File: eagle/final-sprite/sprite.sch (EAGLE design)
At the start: 40 parts

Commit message: merged final-sprite changes into master branch
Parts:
- removed 32KHZ: SPRITECRYSTALSPRITECRYSTAL, SpriteCrystal:SPRITECRYSTALSPRITECRYSTAL
- removed ANTENNA1, ANTENNA2: ANTENNA, SpriteAntenna:ANTENNA
- removed C12: 10uF, SparkFun:CAP0805
- removed CC430: CC430F513X---RGZ48, TI_MSP430_v16:CC430F513X---RGZ48
- removed GNDPIN, VCCPIN: SPRITE_PIN, SpritePin:SPRITE_PIN
- removed H-BRIDGE: LV8417CS, lv8417cs:LV8417CS
- removed JP1: (no value), SparkFun:M02PTH
- removed LED1: (no value), SparkFun:LED0603
- removed RECTIFIER: NSR1030QMUTAG, NSR1030QMUTAG:NSR1030QMUTAG
- removed TRISOL1, TRISOL2, TRISOL3, TRISOL4: TRISOLX-WING, TriSolX_QzQube:TRISOLX-WING
- removed TXCO: (no value), SpriteTCXO:TCXO_7Z
- added ANT-N, ANT-P: ANTENNA, SpriteAntenna:ANTENNA
- added D1: (no value), SparkFun:LED0603
- added JP2: (no value), SparkFun:M02PTH
- added P1, P2: SPRITE_PIN, SpritePin:SPRITE_PIN
- added S1, S2, S3, S4: TRISOLX-WING, TriSolX_QzQube:TRISOLX-WING
- added U$1: UMAC, UMAC:UMAC
- added U$4: ADP5092, STAC:ADP5092
- added U1: CC430F5137, TI_MSP430_v16:CC430F513X---RGZ48
- added X1: TCXO_7Z, SpriteTCXO:TCXO_7Z
- C1: value 0.1uF -> 10 nF; device SparkFun:CAP0805 -> SparkFun:CAP0603-CAP
- C10: value 470nF -> 0.1uF
- C11: value 10nF -> 10uF
- C2: value 10nF -> 470nF; device SparkFun:CAP0805 -> SparkFun:CAP0603-CAP
- C3: value 0.1uF -> 470nF; device SparkFun:CAP0805 -> SparkFun:CAP0603-CAP
- C4: value 0.1uF -> 2.2nF; device SparkFun:CAP0805 -> SparkFun:CAP0603-CAP
- C5: value 10uF -> 10nF; device SparkFun:CAP0805 -> SparkFun:CAP0603-CAP
- C6: value 470nF -> 100nF; device SparkFun:CAP0805 -> SparkFun:CAP0603-CAP
- C7: value 10uF -> 0.1uF
- L1: value 12nH -> 12 nH; device SparkFun:INDUCTOR0402 -> SparkFun:INDUCTOR0603
- R1: value 10K -> 56K; device SparkFun:RESISTOR0805-RES -> SparkFun:RESISTOR0603-RES
- R2: value 10K -> 47K; device SparkFun:RESISTOR0805-RES -> SparkFun:RESISTOR0603-RES
- R5: value 10K -> 270R; device SparkFun:RESISTOR0805-RES -> SparkFun:RESISTOR0603-RES
- R6, R7: value 56K -> 10K
- R8: value 1K -> 10K
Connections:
- removed net #RST/SBWTDIO: CC430.40, JP3.1, R7.2
- removed net ANT1: ANTENNA1.IN, CC430.29
- removed net ANT2: ANTENNA2.IN, CC430.30
- removed net COIL1: H-BRIDGE.OUT1, R8.1, RECTIFIER.PIN1
- removed net GUARD: C10.1, C8.1, C9.1, CC430.27, CC430.28, CC430.31, CC430.32, CC430.34, L1.2
- removed net LOADLINE: H-BRIDGE.OUT2, R8.2, RECTIFIER.PIN3
- removed net N$8: 32KHZ.PIN1, CC430.43
- removed net P1.0: CC430.13
- removed net P1.1: CC430.12
- removed net P1.2: CC430.11
- removed net P1.7: CC430.4
- removed net P2.1/A1: CC430.2
- removed net P2.2/A2: CC430.1
- removed net P2.2/A4: CC430.47
- removed net P2.3/A3: CC430.48
- removed net P2.6: CC430.24
- removed net P2.7: CC430.23, H-BRIDGE.IN2
- removed net P3.0: CC430.21, H-BRIDGE.IN1
- removed net P3.1: CC430.20, H-BRIDGE.ENA
- removed net P3.2: CC430.19
- removed net P3.3: CC430.18
- removed net P3.4: CC430.17
- removed net P3.5: CC430.16
- removed net P3.6: CC430.15
- removed net P3.7: CC430.14, LED1.A
- removed net R_BIAS: CC430.33, R6.2
- removed net TCK_PJ.3: CC430.38
- removed net TDI_PJ.1: CC430.36
- removed net TDO_PJ.0: CC430.35
- removed net TEST/SBWTCK: CC430.39, JP3.2
- removed net TMS_PJ.2: CC430.37
- removed net VCORE: C6.2, CC430.7
- new net N$11: D1.A, R5.1
- new net N$12: C1.2, X1.OUT
- new net N$6: C8.1, LSM9DS1.CAP
- new net PGOOD: U$4.PGOOD
- new net REGGOOD: U$4.REGGOOD
- new net RF_N: ANT-N.IN, U1.30
- new net RF_P: ANT-P.IN, U1.29
- new net RST: C4.2, JP2.1, R2.1, U1.40
- new net TST: JP2.2, U1.39
- new net VBAT: U$1.V+, U$4.BAT
- new net VCCA: C5.1, C6.1, L1.2, U1.27, U1.28, U1.31, U1.32
- new net VCCINT: S1.C, S2.C, S3.C, S4.C
- new net VCCIO: U$4.REGFB, U$4.REG_OUT
- net GND: now also C11.2, C4.1, C6.2, C7.2, D1.C, P2.PIN, R1.2, R7.1, R8.1, S1.A, S2.A, S3.A, S4.A, U$1.V-, U$4.AGND, U$4.GND, U$4.PGND, U1.42, U1.49, X1.GND; no longer C1.2, C12.1, C4.2, C6.1, C7.1, CC430.42, CC430.49, GNDPIN.P$1, H-BRIDGE.PGND, H-BRIDGE.SGND, LED1.C, R4.1, R5.1, R6.1, RECTIFIER.GND, TRISOL1.A, TRISOL2.A, TRISOL3.A, TRISOL4.A, TXCO.GND
- net N$1: now also U1.25; no longer LSM9DS1.C1
- net N$2: now also R5.2, U1.14; no longer C2.1, LSM9DS1.CAP
- net N$3: now also U1.33; no longer LSM9DS1.CS_A/G, LSM9DS1.CS_M, LSM9DS1.SDO_A/G, LSM9DS1.SDO_M
- net N$4: now also C3.1, U1.7; no longer C11.1, CC430.25
- net N$5: now also C7.1, LSM9DS1.C1; no longer C11.2, TXCO.OUT
- net N$7: now also LSM9DS1.CS_A/G, LSM9DS1.CS_M, LSM9DS1.SDO_A/G, LSM9DS1.SDO_M, R3.1; no longer 32KHZ.PIN2, CC430.44
- net P2.0/A0: now also R7.2; no longer CC430.3, R4.2
- net P2.5/A5: now also R8.2; no longer CC430.46, R5.2
- net SCL: now also R6.1, U1.9; no longer CC430.9, R3.1
- net SDA: now also R4.1, U1.10; no longer CC430.10, R2.1
- net UART_RX: now also JP3.2, U1.6; no longer CC430.6, JP1.2
- net UART_TX: now also JP3.1, U1.5; no longer CC430.5, JP1.1
- net VCC: now also C10.1, C11.1, C2.1, C9.1, P1.PIN, R4.2, R6.2, U$4.SYS, U1.22, U1.34, U1.41, U1.45, U1.8, X1.VCC; no longer C12.2, C3.1, C4.1, C5.1, C7.2, CC430.22, CC430.41, CC430.45, CC430.8, H-BRIDGE.VCC, H-BRIDGE.VM, R1.2, R7.1, RECTIFIER.VCC, TRISOL1.C, TRISOL2.C, TRISOL3.C, TRISOL4.C, TXCO.VCC, VCCPIN.P$1
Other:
- note added: "CORE:"
- note added: "Power"
- note added: "Torque Coils"
- note removed: "Antennae"
- note removed: "CDH/T&C:"
- note removed: "Inductive Powering/Torque Coils"
- note removed: "Power/Attitude Control:"
- note removed: "The CC430 serves as both flight computer and radio. It is connected via I2C to the LSM9DS1 and via analog input to the two sun sensors (phototransistors). The MCU is also connected to an external 32.678 kHz oscillator, and a 26 MHz clock. The layout is schematically identical to a PanStamp NRG 2, and is programmable via SBW or serial. The CC430 connects with the dipole antennae."
- note removed: "The LMS9DS1 is connected via I2C to the CC430. The chip includes a magnetometer (3-axis), an accelerometer (3-axis), and a gyroscope (3-axis). SparkFun has written supporting Arduino libraries. The sun sensors are two ALS-PT19-315C ambient light sensors"
- note removed: "The board features four TriSolX solar panels, along with a set of inductive coils and a full bridge rectifier for inductive powering. The inductive coils double as torque coils, controlled via four of the CC430 pins connected to an H-bridge."
- note removed: "The output pins of the H-Bridge are connected with the coils as the load. The coils are connected in parallel to the full bridge rectifier circuit."
- note removed: "TriSolX Solar Panels"

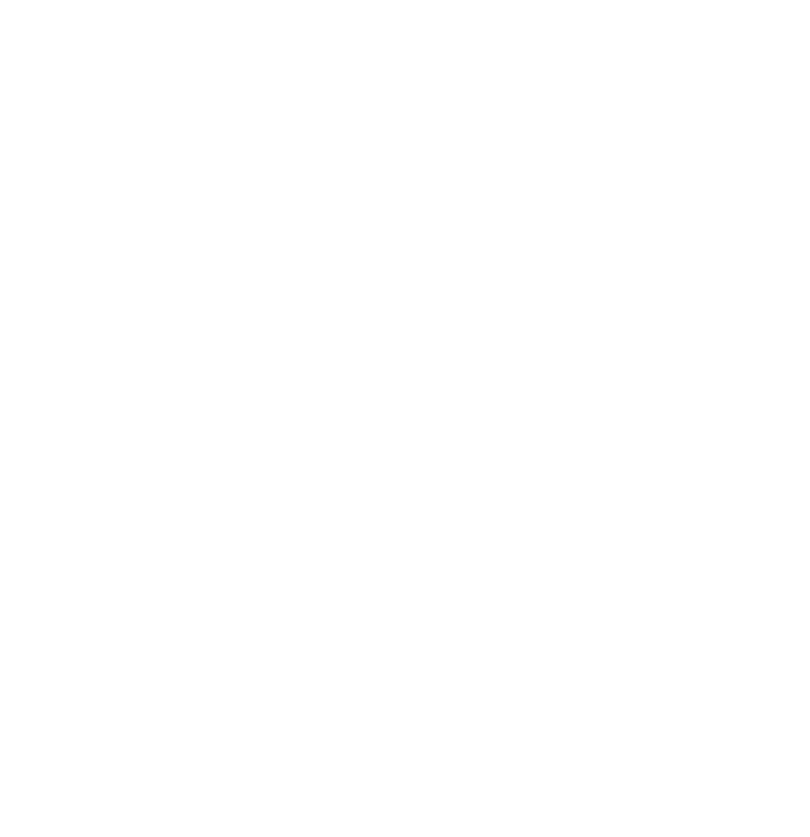
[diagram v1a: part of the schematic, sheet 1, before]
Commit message: Add DRV8833CRTER
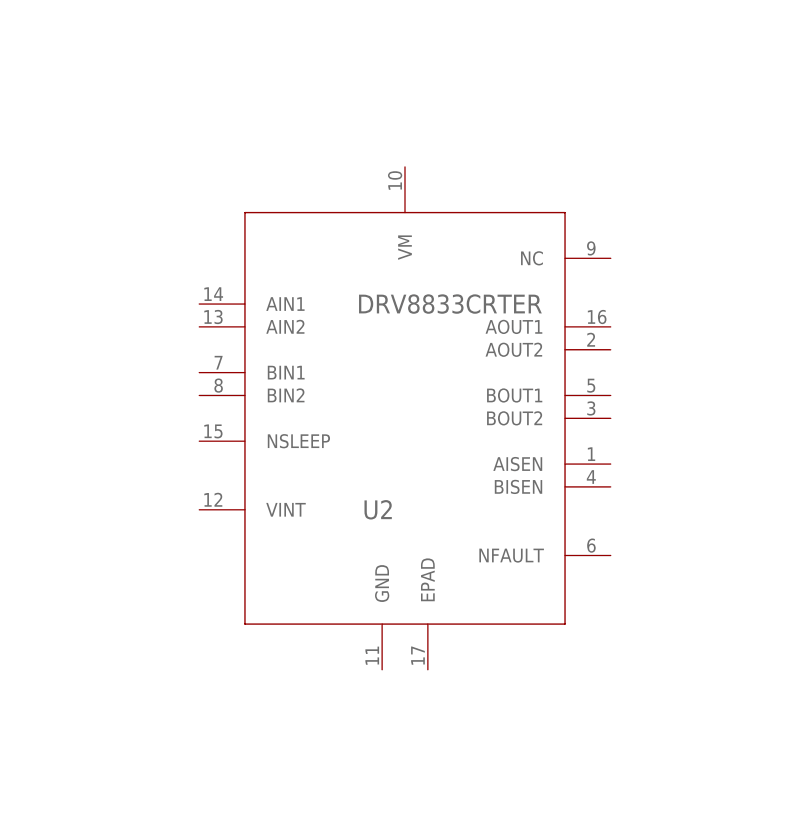
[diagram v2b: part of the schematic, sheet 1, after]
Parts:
- added U2: DRV8833CRTER, STAC:DRV8833CRTER
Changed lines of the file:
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@@
 <?xml version="1.0" encoding="utf-8"?>
 <!DOCTYPE eagle SYSTEM "eagle.dtd">
-<eagle version="9.0.1">
+<eagle version="9.0.0">
 <drawing>
 <settings>
@@
 <part name="P+1" library="SparkFun" deviceset="VCC" device=""/>
 <part name="SUPPLY1" library="SparkFun-PowerSymbols" library_urn="urn:adsk.eagle:library:530" deviceset="VCCIO" device=""/>
+<part name="U2" library="STAC" deviceset="DRV8833CRTER" device=""/>
 </parts>
 <sheets>
@@
 <instance part="P+1" gate="1" x="226.06" y="-78.74"/>
 <instance part="SUPPLY1" gate="G$1" x="220.98" y="-78.74"/>
+<instance part="U2" gate="A" x="203.2" y="-218.44"/>
 </instances>
 <busses>

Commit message: Place COIL?_IN? pins
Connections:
- new net COIL1_IN1: U1.20
- new net COIL1_IN2: U1.19
- new net COIL2_IN1: U1.18
- new net COIL2_IN2: U1.17
- new net COIL3_IN1: U1.2
- new net COIL3_IN2: U1.1
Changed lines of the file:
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@@
+</segment>
+</net>
+<net name="COIL1_IN1" class="0">
+<segment>
+<pinref part="U1" gate="G$1" pin="20"/>
+<wire x1="-20.32" y1="-236.22" x2="-33.02" y2="-236.22" width="0.1524" layer="91"/>
+<label x="-33.02" y="-236.22" size="1.778" layer="95"/>
+</segment>
+</net>
+<net name="COIL1_IN2" class="0">
+<segment>
+<pinref part="U1" gate="G$1" pin="19"/>
+<wire x1="-20.32" y1="-233.68" x2="-33.02" y2="-233.68" width="0.1524" layer="91"/>
+<label x="-33.02" y="-233.68" size="1.778" layer="95"/>
+</segment>
+</net>
+<net name="COIL2_IN1" class="0">
+<segment>
+<pinref part="U1" gate="G$1" pin="18"/>
+<wire x1="-20.32" y1="-231.14" x2="-33.02" y2="-231.14" width="0.1524" layer="91"/>
+<label x="-33.02" y="-231.14" size="1.778" layer="95"/>
+</segment>
+</net>
+<net name="COIL2_IN2" class="0">
+<segment>
+<pinref part="U1" gate="G$1" pin="17"/>
+<wire x1="-20.32" y1="-228.6" x2="-33.02" y2="-228.6" width="0.1524" layer="91"/>
+<label x="-33.02" y="-228.6" size="1.778" layer="95"/>
+</segment>
+</net>
+<net name="COIL3_IN1" class="0">
+<segment>
+<pinref part="U1" gate="G$1" pin="2"/>
+<wire x1="-20.32" y1="-190.5" x2="-33.02" y2="-190.5" width="0.1524" layer="91"/>
+<label x="-33.02" y="-190.5" size="1.778" layer="95"/>
+</segment>
+</net>
+<net name="COIL3_IN2" class="0">
+<segment>
+<pinref part="U1" gate="G$1" pin="1"/>
+<wire x1="-20.32" y1="-187.96" x2="-33.02" y2="-187.96" width="0.1524" layer="91"/>
+<label x="-33.02" y="-187.96" size="1.778" layer="95"/>
 </segment>
 </net>

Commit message: More progress on COIL12
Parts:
- added C12: 10uF, SparkFun:CAP0603-CAP
- added C13: 2.2uF, SparkFun:CAP0603-CAP
- added R10, R9: 270R, SparkFun:RESISTOR0603-RES
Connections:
- new net COIL12_EN: U1.16, U2.NSLEEP
- new net COIL12_FAULT: U1.13, U2.NFAULT
- new net COIL3_EN: U1.48
- new net COIL3_FAULT: U1.12
- new net N$10: R10.2, U2.AISEN
- new net N$8: C13.1, U2.VINT
- new net N$9: R9.2, U2.BISEN
- net COIL1_IN1: now also U2.AIN1
- net COIL1_IN2: now also U2.AIN2
- net COIL2_IN1: now also U2.BIN1
- net COIL2_IN2: now also U2.BIN2
- net GND: now also C12.2, C13.2, R10.1, R9.1, U2.EPAD, U2.GND
- net VCCIO: now also C12.1, U2.VM
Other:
- note added: "Rated up to VCCIO"
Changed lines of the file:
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@@
 <part name="SUPPLY1" library="SparkFun-PowerSymbols" library_urn="urn:adsk.eagle:library:530" deviceset="VCCIO" device=""/>
 <part name="U2" library="STAC" deviceset="DRV8833CRTER" device=""/>
+<part name="GND17" library="SparkFun" deviceset="GND" device=""/>
+<part name="SUPPLY2" library="SparkFun-PowerSymbols" library_urn="urn:adsk.eagle:library:530" deviceset="VCCIO" device=""/>
+<part name="C12" library="SparkFun" deviceset="CAP" device="0603-CAP" value="10uF"/>
+<part name="GND18" library="SparkFun" deviceset="GND" device=""/>
+<part name="C13" library="SparkFun" deviceset="CAP" device="0603-CAP" value="2.2uF"/>
+<part name="GND19" library="SparkFun" deviceset="GND" device=""/>
+<part name="R9" library="SparkFun" deviceset="RESISTOR" device="0603-RES" value="270R"/>
+<part name="R10" library="SparkFun" deviceset="RESISTOR" device="0603-RES" value="270R"/>
+<part name="GND24" library="SparkFun" deviceset="GND" device=""/>
+<part name="GND25" library="SparkFun" deviceset="GND" device=""/>
 </parts>
 <sheets>
@@
 <text x="152.4" y="-73.66" size="5.08" layer="97">Power</text>
 <wire x1="149.86" y1="-167.64" x2="304.8" y2="-167.64" width="0.6096" layer="97" style="longdash"/>
+<text x="187.96" y="-248.92" size="1.778" layer="91">Rated up to VCCIO</text>
 </plain>
 <instances>
@@
 <instance part="SUPPLY1" gate="G$1" x="220.98" y="-78.74"/>
 <instance part="U2" gate="A" x="203.2" y="-218.44"/>
+<instance part="GND17" gate="1" x="228.6" y="-269.24" rot="MR0"/>
+<instance part="SUPPLY2" gate="G$1" x="213.36" y="-195.58"/>
+<instance part="C12" gate="G$1" x="213.36" y="-200.66"/>
+<instance part="GND18" gate="1" x="213.36" y="-205.74" rot="MR0"/>
+<instance part="C13" gate="G$1" x="198.12" y="-254"/>
+<instance part="GND19" gate="1" x="198.12" y="-259.08" rot="MR0"/>
+<instance part="R9" gate="G$1" x="256.54" y="-259.08" rot="R90"/>
+<instance part="R10" gate="G$1" x="266.7" y="-256.54" rot="R90"/>
+<instance part="GND24" gate="1" x="256.54" y="-269.24" rot="MR0"/>
+<instance part="GND25" gate="1" x="266.7" y="-269.24" rot="MR0"/>
 </instances>
 <busses>
@@
 <pinref part="GND3" gate="1" pin="GND"/>
 </segment>
+<segment>
+<pinref part="U2" gate="A" pin="GND"/>
+<wire x1="226.06" y1="-261.62" x2="226.06" y2="-264.16" width="0.1524" layer="91"/>
+<wire x1="226.06" y1="-264.16" x2="228.6" y2="-264.16" width="0.1524" layer="91"/>
+<pinref part="U2" gate="A" pin="EPAD"/>
+<wire x1="228.6" y1="-264.16" x2="231.14" y2="-264.16" width="0.1524" layer="91"/>
+<wire x1="231.14" y1="-264.16" x2="231.14" y2="-261.62" width="0.1524" layer="91"/>
+<wire x1="228.6" y1="-264.16" x2="228.6" y2="-266.7" width="0.1524" layer="91"/>
+<pinref part="GND17" gate="1" pin="GND"/>
+</segment>
+<segment>
+<pinref part="C12" gate="G$1" pin="2"/>
+<pinref part="GND18" gate="1" pin="GND"/>
+</segment>
+<segment>
+<pinref part="C13" gate="G$1" pin="2"/>
+<pinref part="GND19" gate="1" pin="GND"/>
+</segment>
+<segment>
+<pinref part="R9" gate="G$1" pin="1"/>
+<pinref part="GND24" gate="1" pin="GND"/>
+<wire x1="256.54" y1="-264.16" x2="256.54" y2="-266.7" width="0.1524" layer="91"/>
+</segment>
+<segment>
+<pinref part="R10" gate="G$1" pin="1"/>
+<pinref part="GND25" gate="1" pin="GND"/>
+<wire x1="266.7" y1="-261.62" x2="266.7" y2="-266.7" width="0.1524" layer="91"/>
+</segment>
 </net>
 <net name="UART_RX" class="0">
@@
 <pinref part="SUPPLY1" gate="G$1" pin="VCCIO"/>
 </segment>
+<segment>
+<pinref part="C12" gate="G$1" pin="1"/>
+<pinref part="SUPPLY2" gate="G$1" pin="VCCIO"/>
+<wire x1="213.36" y1="-195.58" x2="228.6" y2="-195.58" width="0.1524" layer="91"/>
+<pinref part="U2" gate="A" pin="VM"/>
+<wire x1="228.6" y1="-195.58" x2="228.6" y2="-205.74" width="0.1524" layer="91"/>
+</segment>
 </net>
 <net name="COIL1_IN1" class="0">
@@
 <label x="-33.02" y="-236.22" size="1.778" layer="95"/>
 </segment>
+<segment>
+<pinref part="U2" gate="A" pin="AIN1"/>
+<wire x1="205.74" y1="-220.98" x2="187.96" y2="-220.98" width="0.1524" layer="91"/>
+<label x="187.96" y="-220.98" size="1.778" layer="95"/>
+</segment>
 </net>
 <net name="COIL1_IN2" class="0">
@@
 <label x="-33.02" y="-233.68" size="1.778" layer="95"/>
 </segment>
+<segment>
+<pinref part="U2" gate="A" pin="AIN2"/>
+<wire x1="205.74" y1="-223.52" x2="187.96" y2="-223.52" width="0.1524" layer="91"/>
+<label x="187.96" y="-223.52" size="1.778" layer="95"/>
+</segment>
 </net>
 <net name="COIL2_IN1" class="0">
@@
 <label x="-33.02" y="-231.14" size="1.778" layer="95"/>
 </segment>
+<segment>
+<pinref part="U2" gate="A" pin="BIN1"/>
+<wire x1="205.74" y1="-228.6" x2="187.96" y2="-228.6" width="0.1524" layer="91"/>
+<label x="187.96" y="-228.6" size="1.778" layer="95"/>
+</segment>
 </net>
 <net name="COIL2_IN2" class="0">
@@
 <label x="-33.02" y="-228.6" size="1.778" layer="95"/>
 </segment>
+<segment>
+<pinref part="U2" gate="A" pin="BIN2"/>
+<wire x1="205.74" y1="-231.14" x2="187.96" y2="-231.14" width="0.1524" layer="91"/>
+<label x="187.96" y="-231.14" size="1.778" layer="95"/>
+</segment>
 </net>
 <net name="COIL3_IN1" class="0">
@@
 </segment>
 </net>
+<net name="N$8" class="0">
+<segment>
+<pinref part="C13" gate="G$1" pin="1"/>
+<wire x1="198.12" y1="-248.92" x2="198.12" y2="-243.84" width="0.1524" layer="91"/>
+<pinref part="U2" gate="A" pin="VINT"/>
+<wire x1="198.12" y1="-243.84" x2="205.74" y2="-243.84" width="0.1524" layer="91"/>
+</segment>
+</net>
+<net name="COIL12_EN" class="0">
+<segment>
+<pinref part="U1" gate="G$1" pin="16"/>
+<wire x1="-20.32" y1="-226.06" x2="-33.02" y2="-226.06" width="0.1524" layer="91"/>
+<label x="-33.02" y="-226.06" size="1.778" layer="95"/>
+</segment>
+<segment>
+<pinref part="U2" gate="A" pin="NSLEEP"/>
+<wire x1="205.74" y1="-236.22" x2="187.96" y2="-236.22" width="0.1524" layer="91"/>
+<label x="187.96" y="-236.22" size="1.778" layer="95"/>
+</segment>
+</net>
+<net name="COIL3_EN" class="0">
+<segment>
+<pinref part="U1" gate="G$1" pin="48"/>
+<wire x1="25.4" y1="-187.96" x2="40.64" y2="-187.96" width="0.1524" layer="91"/>
+<label x="30.48" y="-187.96" size="1.778" layer="95"/>
+</segment>
+</net>
+<net name="COIL12_FAULT" class="0">
+<segment>
+<pinref part="U1" gate="G$1" pin="13"/>
+<wire x1="-20.32" y1="-218.44" x2="-38.1" y2="-218.44" width="0.1524" layer="91"/>
+<label x="-38.1" y="-218.44" size="1.778" layer="95"/>
+</segment>
+<segment>
+<pinref part="U2" gate="A" pin="NFAULT"/>
+<wire x1="251.46" y1="-248.92" x2="279.4" y2="-248.92" width="0.1524" layer="91"/>
+<label x="287.02" y="-246.38" size="1.778" layer="95" rot="R180"/>
+<wire x1="279.4" y1="-248.92" x2="287.02" y2="-248.92" width="0.1524" layer="91"/>
+</segment>
+</net>
+<net name="COIL3_FAULT" class="0">
+<segment>
+<pinref part="U1" gate="G$1" pin="12"/>
+<wire x1="-20.32" y1="-215.9" x2="-38.1" y2="-215.9" width="0.1524" layer="91"/>
+<label x="-38.1" y="-215.9" size="1.778" layer="95"/>
+</segment>
+</net>
+<net name="N$9" class="0">
+<segment>
+<pinref part="R9" gate="G$1" pin="2"/>
+<pinref part="U2" gate="A" pin="BISEN"/>
+<wire x1="256.54" y1="-254" x2="256.54" y2="-241.3" width="0.1524" layer="91"/>
+<wire x1="256.54" y1="-241.3" x2="251.46" y2="-241.3" width="0.1524" layer="91"/>
+</segment>
+</net>
+<net name="N$10" class="0">
+<segment>
+<pinref part="R10" gate="G$1" pin="2"/>
+<pinref part="U2" gate="A" pin="AISEN"/>
+<wire x1="266.7" y1="-251.46" x2="266.7" y2="-238.76" width="0.1524" layer="91"/>
+<wire x1="266.7" y1="-238.76" x2="251.46" y2="-238.76" width="0.1524" layer="91"/>
+</segment>
+</net>
